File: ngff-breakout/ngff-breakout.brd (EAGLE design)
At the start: 90 x 80 mm, 77 parts, among them U2 LD1085D2T33R, X1 PINHD-2X4, X7 694108106102, X9 ZX360D-B-10P(30), Y4 MHF4, Y5 MHF4, Y6 MHF4

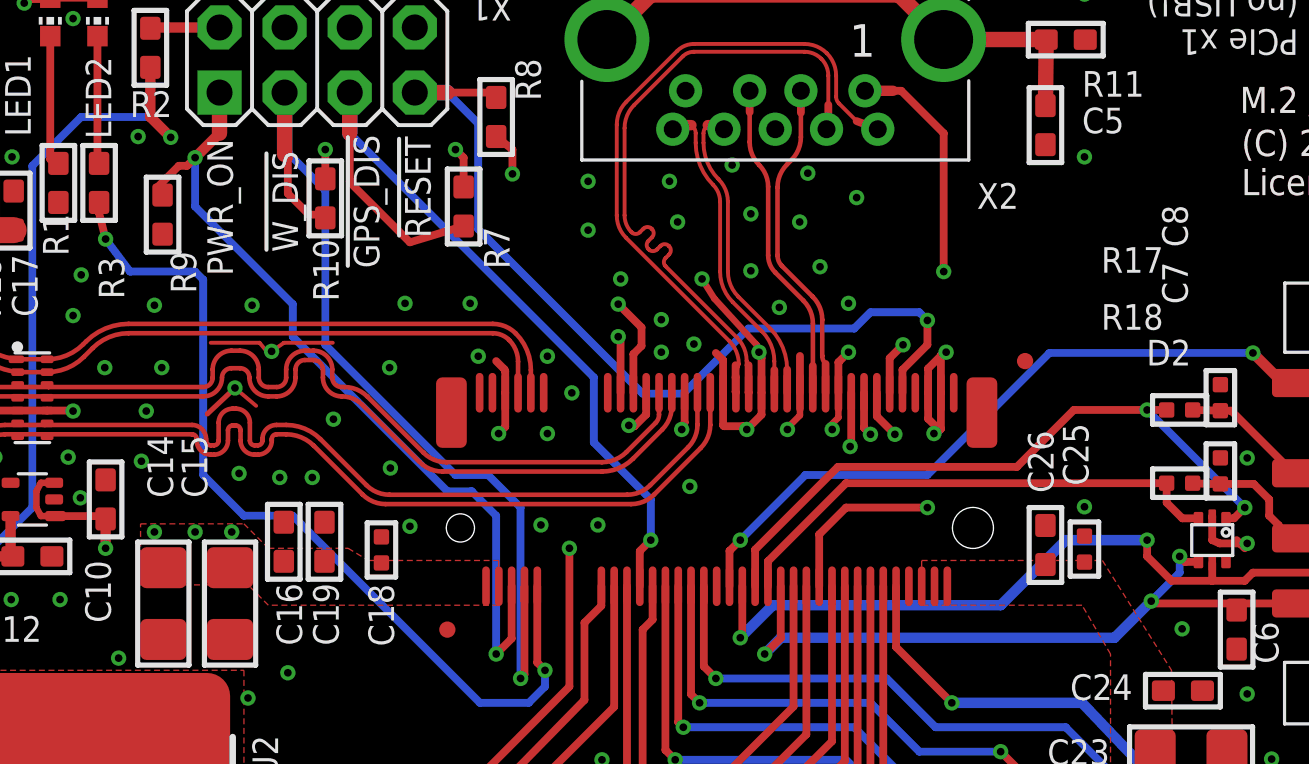
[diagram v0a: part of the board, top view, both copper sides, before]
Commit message: ngff: set R9 to 100k (solves OS#4209)
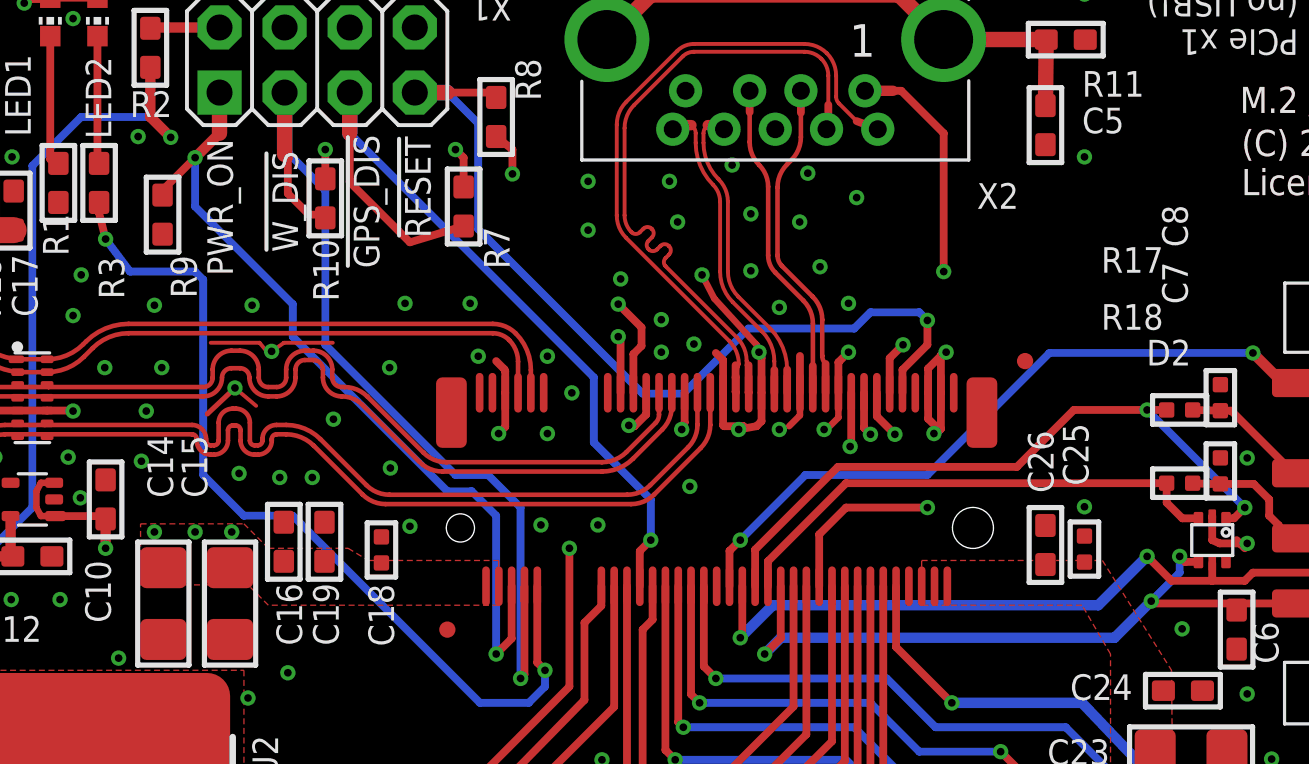
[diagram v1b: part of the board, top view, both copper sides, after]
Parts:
- R9: value 10k -> 100k
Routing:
- net _USIM2_DATA: track 58.5 -> 57.6 mm
- net GND: track 49.2 -> 49.8 mm
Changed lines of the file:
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@@
 <attribute name="VALUE" x="23.0823" y="69.215" size="0.508" layer="27" font="vector" ratio="10" rot="R90"/>
-</element>
-<element name="R9" library="rc-sysmocom" package="_0603" value="10k" x="15.24" y="70.1675" smashed="yes" rot="R90">
-<attribute name="DESCRIPTION" value="RES 10K OHM 1%% 1/10W 0603" x="15.24" y="70.1675" size="1" layer="27" ratio="16" rot="R90" display="off"/>
-<attribute name="LINK" value="https://www.digikey.de/product-detail/de/stackpole-electronics-inc/RMCF0603FT10K0/RMCF0603FT10K0CT-ND" x="15.24" y="70.1675" size="1" layer="27" ratio="16" rot="R90" display="off"/>
-<attribute name="MANUFACTURERPARTNUMBER" value="RMCF0603FT10K0" x="15.24" y="70.1675" size="1" layer="27" ratio="16" rot="R90" display="off"/>
-<attribute name="CLASS" value="RESISTOR" x="15.24" y="70.1675" size="1" layer="27" ratio="16" rot="R90" display="off"/>
-<attribute name="POPULATED" value="TRUE" x="15.24" y="70.1675" size="1" layer="27" ratio="16" rot="R90" display="off"/>
-<attribute name="SOURCE" value="DIGIKEY" x="15.24" y="70.1675" size="1" layer="27" ratio="16" rot="R90" display="off"/>
-<attribute name="ROHSCERTIFICATE" value="UNKNOWN ROHS CERTIFICATE" x="15.24" y="70.1675" size="1" layer="27" ratio="16" rot="R90" display="off"/>
-<attribute name="MANUFACTURER" value="Stackpole Electronics Inc" x="15.24" y="70.1675" size="1" layer="27" ratio="16" rot="R90" display="off"/>
-<attribute name="SOURCEPARTNUMBER" value="RMCF0603FT10K0CT-ND" x="15.24" y="70.1675" size="1" layer="27" ratio="16" rot="R90" display="off"/>
-<attribute name="NAME" x="15.5575" y="68.73875" size="1" layer="25" font="vector" ratio="16" rot="R270"/>
-<attribute name="VALUE" x="16.7323" y="68.58" size="0.508" layer="27" font="vector" ratio="10" rot="R90"/>
 </element>
 <element name="R4" library="rc-sysmocom" package="_0603" value="DNP" x="75.8825" y="27.305" smashed="yes">
@@
 <element name="FID1" library="dicons" package="VISION_REF15" value="" x="81.5" y="2.54" smashed="yes"/>
 <element name="FID2" library="dicons" package="VISION_REF15" value="" x="8.5" y="2.54" smashed="yes"/>
+<element name="R9" library="rc-sysmocom" package="_0603" value="100k" x="15.24" y="70.1675" smashed="yes" rot="R90">
+<attribute name="SOURCE" value="DIGIKEY" x="15.24" y="70.1675" size="1.778" layer="27" rot="R90" display="off"/>
+<attribute name="CLASS" value="RESISTOR" x="15.24" y="70.1675" size="1.778" layer="27" rot="R90" display="off"/>
+<attribute name="MANUFACTURER" value="Vishay Dale" x="15.24" y="70.1675" size="1.778" layer="27" rot="R90" display="off"/>
+<attribute name="ROHSCERTIFICATE" value="Bleifrei / RoHS-konform" x="15.24" y="70.1675" size="1.778" layer="27" rot="R90" display="off"/>
+<attribute name="LINK" value="https://www.digikey.de/product-detail/de/vishay-dale/CRCW0603100KFKEA/541-100KHCT-ND" x="15.24" y="70.1675" size="1.778" layer="27" rot="R90" display="off"/>
+<attribute name="MANUFACTURERPARTNUMBER" value="CRCW0603100KFKEA" x="15.24" y="70.1675" size="1.778" layer="27" rot="R90" display="off"/>
+<attribute name="POPULATED" value="TRUE" x="15.24" y="70.1675" size="1.778" layer="27" rot="R90" display="off"/>
+<attribute name="DESCRIPTION" value="RES SMD 100K OHM 1%% 1/10W 0603" x="15.24" y="70.1675" size="1.778" layer="27" rot="R90" display="off"/>
+<attribute name="SOURCEPARTNUMBER" value="541-100KHCT-ND" x="15.24" y="70.1675" size="1.778" layer="27" rot="R90" display="off"/>
+<attribute name="NAME" x="15.5575" y="68.58" size="1.016" layer="25" font="vector" ratio="14" rot="R270"/>
+<attribute name="VALUE" x="16.7323" y="68.58" size="0.508" layer="27" font="vector" ratio="10" rot="R90"/>
+</element>
 </elements>
 <signals>
@@
 <via x="18.0975" y="79.24675" extent="1-16" drill="0.3"/>
 <via x="38.5125" y="64.8005" extent="1-16" drill="0.3"/>
-<via x="36.29" y="67.658" extent="1-16" drill="0.3"/>
+<via x="36.29" y="67.81675" extent="1-16" drill="0.3"/>
 <via x="35.02" y="71.468" extent="1-16" drill="0.3"/>
 <via x="35.3375" y="69.8805" extent="1-16" drill="0.3"/>
@@
 <via x="42.005" y="64.8005" extent="1-16" drill="0.3"/>
 <via x="42.005" y="66.7055" extent="1-16" drill="0.3"/>
-<via x="41.37" y="61.78425" extent="1-16" drill="0.3"/>
-<via x="39.62375" y="61.78425" extent="1-16" drill="0.3"/>
-<via x="38.03625" y="61.78425" extent="1-16" drill="0.3"/>
+<via x="41.0525" y="61.78425" extent="1-16" drill="0.3"/>
+<via x="39.30625" y="61.78425" extent="1-16" drill="0.3"/>
+<via x="37.71875" y="61.78425" extent="1-16" drill="0.3"/>
 <via x="35.81375" y="59.56175" extent="1-16" drill="0.3"/>
 <wire x1="45.1115" y1="63.2175" x2="45.1115" y2="64.1615" width="0.3048" layer="1"/>
 <wire x1="45.1115" y1="64.1615" x2="45.72" y2="64.77" width="0.3048" layer="1"/>
-<contactref element="R9" pad="1"/>
 <via x="12.065" y="67.81675" extent="1-16" drill="0.3"/>
 <via x="67.405" y="50.8305" extent="1-16" drill="0.3"/>
@@
 <wire x1="37.1115" y1="61.9485" x2="37.1475" y2="61.9125" width="0.3048" layer="1"/>
 <wire x1="37.1475" y1="61.9125" x2="37.908" y2="61.9125" width="0.3048" layer="1"/>
-<wire x1="37.908" y1="61.9125" x2="38.03625" y2="61.78425" width="0.3048" layer="1"/>
+<wire x1="37.908" y1="61.9125" x2="37.71875" y2="61.78425" width="0.3048" layer="1"/>
 <via x="35.49625" y="61.78425" extent="1-16" drill="0.3"/>
 <wire x1="35.6115" y1="63.2175" x2="35.6115" y2="62.05825" width="0.3048" layer="1"/>
@@
 <wire x1="54.35625" y1="38.387" x2="54.323" y2="38.387" width="0.3048" layer="1"/>
 <wire x1="54.323" y1="38.387" x2="54.2925" y2="38.4175" width="0.3048" layer="1"/>
-<wire x1="38.6115" y1="63.2175" x2="38.6115" y2="62.3595" width="0.3048" layer="1"/>
-<wire x1="38.6115" y1="62.3595" x2="38.03625" y2="61.78425" width="0.3048" layer="1"/>
+<wire x1="38.6115" y1="63.2175" x2="38.6115" y2="62.1065" width="0.3048" layer="1"/>
+<wire x1="38.6115" y1="62.1065" x2="38.4175" y2="61.9125" width="0.3048" layer="1"/>
+<wire x1="38.4175" y1="61.9125" x2="37.71875" y2="61.78425" width="0.3048" layer="1"/>
 <wire x1="38.6115" y1="63.2175" x2="38.6115" y2="64.576" width="0.3048" layer="1"/>
 <wire x1="38.6115" y1="64.576" x2="38.57625" y2="64.77" width="0.3048" layer="1"/>
-<wire x1="36.29" y1="67.658" x2="36.76625" y2="66.8975" width="0.254" layer="1"/>
+<wire x1="36.29" y1="67.81675" x2="36.76625" y2="66.8975" width="0.254" layer="1"/>
 <wire x1="36.76625" y1="66.8975" x2="38.4175" y2="65.0875" width="0.254" layer="1"/>
 <wire x1="38.4175" y1="65.0875" x2="38.57625" y2="64.77" width="0.254" layer="1"/>
@@
 <wire x1="41.6115" y1="62.249" x2="41.275" y2="61.9125" width="0.254" layer="1"/>
 <via x="42.64" y="1.9355" extent="1-16" drill="0.3"/>
+<contactref element="R9" pad="1"/>
 </signal>
 <signal name="USIM1_POWER" class="3">
@@
 <contactref element="NGFF1" pad="42"/>
 <contactref element="R14" pad="1"/>
-<via x="53.6575" y="57.4675" extent="1-16" drill="0.3"/>
-<wire x1="53.6575" y1="57.4675" x2="50.4825" y2="57.4675" width="0.4064" layer="16"/>
-<wire x1="50.4825" y1="57.4675" x2="47.9425" y2="54.9275" width="0.4064" layer="16"/>
-<wire x1="47.9425" y1="54.9275" x2="39.0525" y2="54.9275" width="0.4064" layer="16"/>
+<via x="53.6575" y="56.8325" extent="1-16" drill="0.3"/>
+<wire x1="53.6575" y1="56.8325" x2="51.7525" y2="54.9275" width="0.4064" layer="16"/>
+<wire x1="51.7525" y1="54.9275" x2="39.0525" y2="54.9275" width="0.4064" layer="16"/>
 <wire x1="39.0525" y1="54.9275" x2="37.7825" y2="53.6575" width="0.4064" layer="16"/>
 <via x="37.7825" y="53.6575" extent="1-16" drill="0.3"/>
@@
 <wire x1="79.0575" y1="53.0225" x2="65.7225" y2="53.0225" width="0.3048" layer="1"/>
 <wire x1="65.7225" y1="53.0225" x2="62.5475" y2="56.1975" width="0.3048" layer="1"/>
-<wire x1="53.6575" y1="57.4675" x2="53.6575" y2="56.8325" width="0.3048" layer="1"/>
 <wire x1="53.6575" y1="56.8325" x2="54.61" y2="55.88" width="0.3048" layer="1"/>
 <wire x1="54.61" y1="55.88" x2="56.1975" y2="55.88" width="0.3048" layer="1"/>
@@
 <wire x1="20.32" y1="66.675" x2="16.51" y2="70.485" width="0.3048" layer="16"/>
 <wire x1="16.51" y1="70.485" x2="16.51" y2="72.39" width="0.3048" layer="16"/>
-<contactref element="R9" pad="2"/>
 <via x="16.51" y="72.39" extent="1-16" drill="0.3"/>
 <contactref element="X1" pad="1"/>
 <wire x1="17.4625" y1="74.93" x2="17.4625" y2="73.3425" width="0.6" layer="1"/>
 <wire x1="17.4625" y1="73.3425" x2="16.51" y2="72.39" width="0.4064" layer="1"/>
-<wire x1="15.24" y1="70.9295" x2="15.0495" y2="71.247" width="0.3048" layer="1"/>
-<wire x1="15.0495" y1="71.247" x2="15.875" y2="72.0725" width="0.3048" layer="1"/>
-<wire x1="15.875" y1="72.0725" x2="16.1925" y2="72.0725" width="0.3048" layer="1"/>
-<wire x1="16.1925" y1="72.0725" x2="16.51" y2="72.39" width="0.3048" layer="1"/>
+<contactref element="R9" pad="2"/>
+<wire x1="16.51" y1="72.39" x2="15.24" y2="71.12" width="0.3048" layer="1"/>
+<wire x1="15.24" y1="71.12" x2="15.24" y2="70.9295" width="0.3048" layer="1"/>
 </signal>
 <signal name="!BODY_SAR">
